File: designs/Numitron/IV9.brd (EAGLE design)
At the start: 59 x 98 mm, 13 parts, among them IC1 TLC5916IN, IC2 TLC5916IN, IC3 TLC5916IN, IC4 TLC5916IN

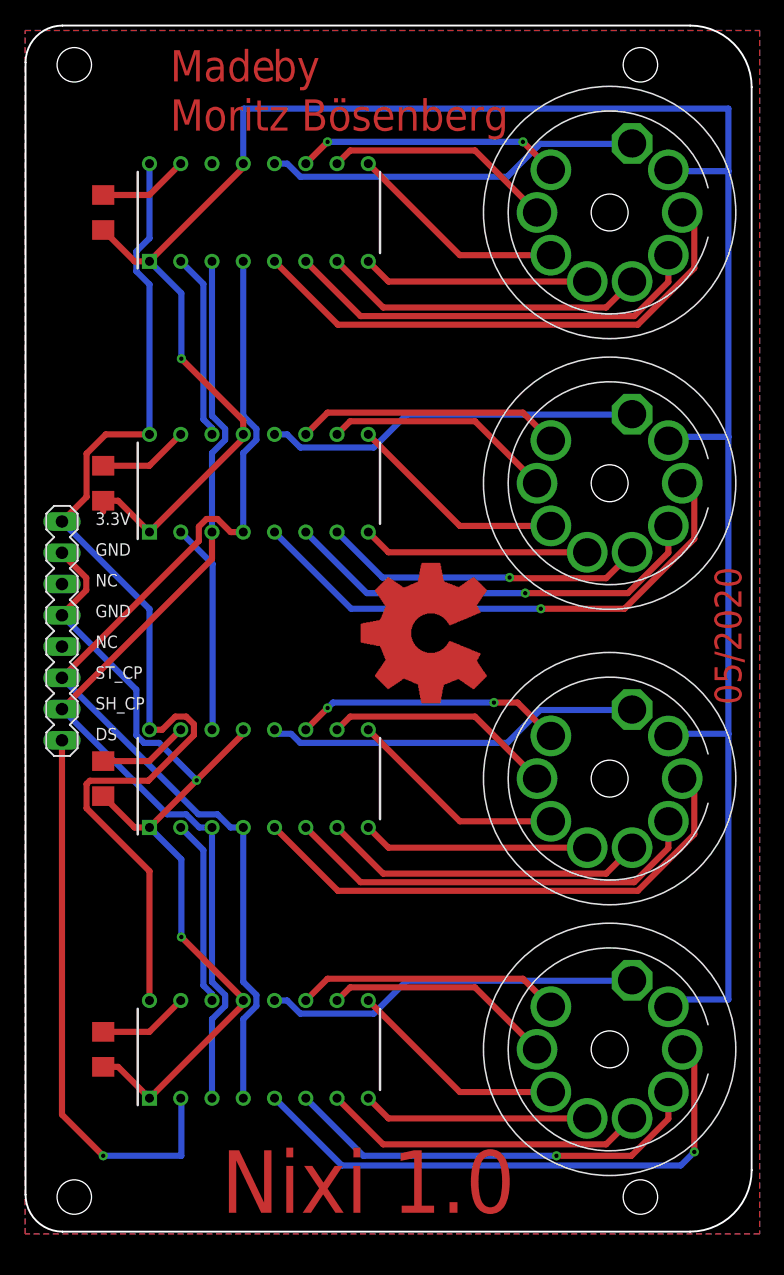
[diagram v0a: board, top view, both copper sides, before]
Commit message: added numitrons for tube clock
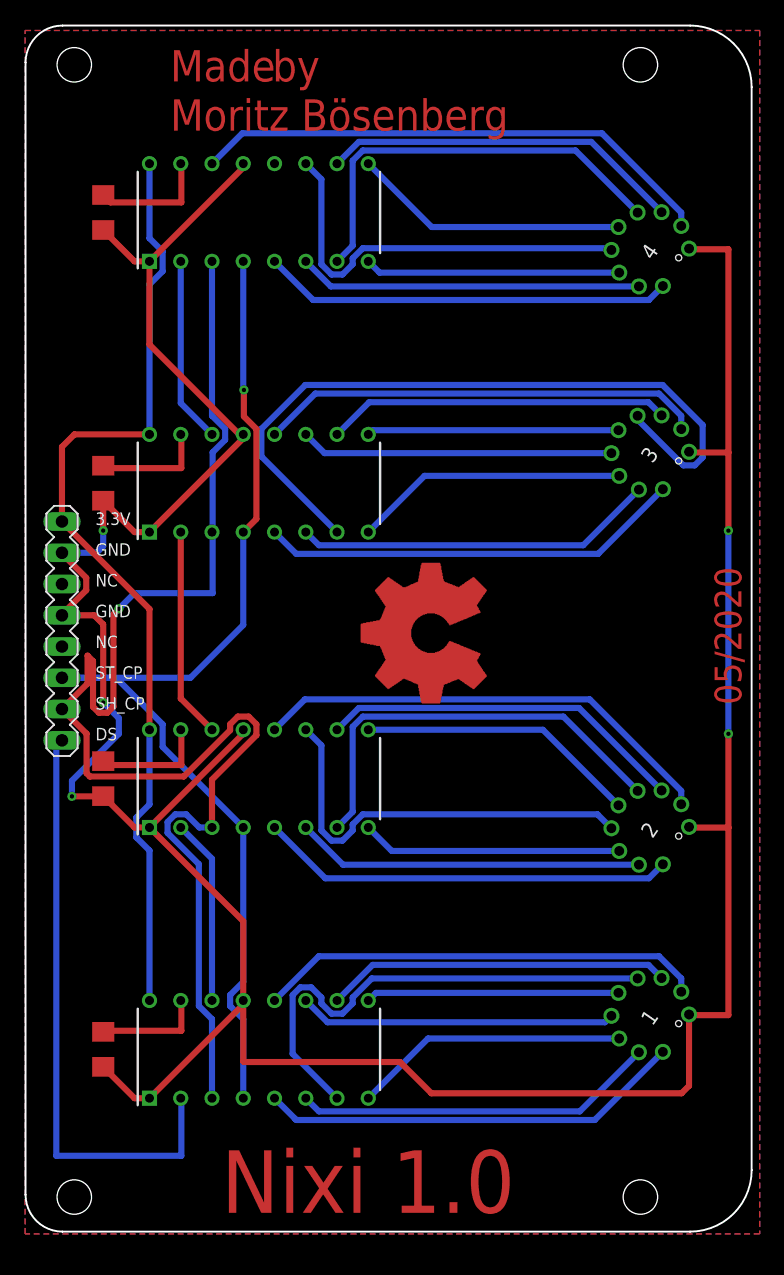
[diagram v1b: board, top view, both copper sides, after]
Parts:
- removed NUMITRON1, NUMITRON2, NUMITRON3, NUMITRON4: (no value), NixieTube:DA-2000
- added 1, 2, 3, 4: IV-9, domestichacks:IV-9
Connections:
- removed net N$1: IC3.8, NUMITRON3.6
- removed net N$10: IC1.10, NUMITRON1.8
- removed net N$11: IC1.11, NUMITRON1.9
- removed net N$12: IC2.5, NUMITRON2.3
- removed net N$14: IC2.6, NUMITRON2.4
- removed net N$2: IC3.9, NUMITRON3.7
- removed net N$3: IC1.5, NUMITRON1.3
- removed net N$33: IC2.7, NUMITRON2.5
- removed net N$34: IC2.8, NUMITRON2.6
- removed net N$37: IC2.9, NUMITRON2.7
- removed net N$38: IC2.10, NUMITRON2.8
- removed net N$39: IC2.11, NUMITRON2.9
- removed net N$4: IC1.6, NUMITRON1.4
- removed net N$40: IC3.5, NUMITRON3.3
- removed net N$41: IC3.6, NUMITRON3.4
- removed net N$42: IC3.7, NUMITRON3.5
- removed net N$43: IC4.5, NUMITRON4.3
- removed net N$44: IC4.6, NUMITRON4.4
- removed net N$45: IC3.10, NUMITRON3.8
- removed net N$46: IC3.11, NUMITRON3.9
- removed net N$47: IC4.7, NUMITRON4.5
- removed net N$5: IC1.7, NUMITRON1.5
- removed net N$50: IC4.10, NUMITRON4.8
- removed net N$51: IC4.11, NUMITRON4.9
- removed net N$6: IC1.8, NUMITRON1.6
- removed net N$7: IC4.8, NUMITRON4.6
- removed net N$8: IC1.9, NUMITRON1.7
- removed net N$9: IC4.9, NUMITRON4.7
- new net A_1: 1.5, IC1.9
- new net A_2: 2.5, IC2.9
- new net A_3: 3.5, IC3.9
- new net A_4: 4.5, IC4.9
- new net B_1: 1.3, IC1.10
- new net B_2: 2.3, IC2.10
- new net B_3: 3.3, IC3.10
- new net B_4: 4.3, IC4.10
- new net C_1: 1.4, IC1.7
- new net C_2: 2.4, IC2.7
- new net C_3: 3.4, IC3.7
- new net C_4: 4.4, IC4.7
- new net D_1: 1.8, IC1.6
- new net D_2: 2.8, IC2.6
- new net D_3: 3.8, IC3.6
- new net D_4: 4.8, IC4.6
- new net E_1: 1.9, IC1.5
- new net E_2: 2.9, IC2.5
- new net E_3: 3.9, IC3.5
- new net E_4: 4.9, IC4.5
- new net F_1: 1.6, IC1.11
- new net F_2: 2.6, IC2.11
- new net F_3: 3.6, IC3.11
- new net F_4: 4.6, IC4.11
- new net G_1: 1.7, IC1.8
- new net G_2: 2.7, IC2.8
- new net G_3: 3.7, IC3.8
- new net G_4: 4.7, IC4.8
- net DEC_1: now also 1.2; no longer NUMITRON1.1
- net DEC_2: now also 2.2; no longer NUMITRON2.1
- net DEC_3: now also 3.2; no longer NUMITRON3.1
- net DEC_4: now also 4.2, IC4.14; no longer IC4.12, NUMITRON4.1
- net GND: now also 1.1, 2.1, 3.1, 4.1; no longer NUMITRON1.2, NUMITRON2.2, NUMITRON3.2, NUMITRON4.2
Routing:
- net C_3: track 0.00 -> 59.7 mm
- net N$3: track 45.6 -> 0.00 mm, vias 1 -> 0
- net N$40: track 44.0 -> 0.00 mm, vias 1 -> 0
- net N$12: track 43.1 -> 0.00 mm
- net N$43: track 43.1 -> 0.00 mm
- net C_1: track 0.00 -> 40.8 mm
- net N$41: track 35.1 -> 0.00 mm, vias 1 -> 0
- net SH_CP: track 81.4 -> 116.4 mm, vias 0 -> 1
- net N$4: track 34.8 -> 0.00 mm, vias 1 -> 0
- net C_2: track 0.00 -> 34.7 mm
- net N$14: track 34.6 -> 0.00 mm
- net N$44: track 34.6 -> 0.00 mm
- net E_1: track 0.00 -> 34.6 mm
- net E_3: track 0.00 -> 34.5 mm
- net C_4: track 0.00 -> 34.3 mm
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
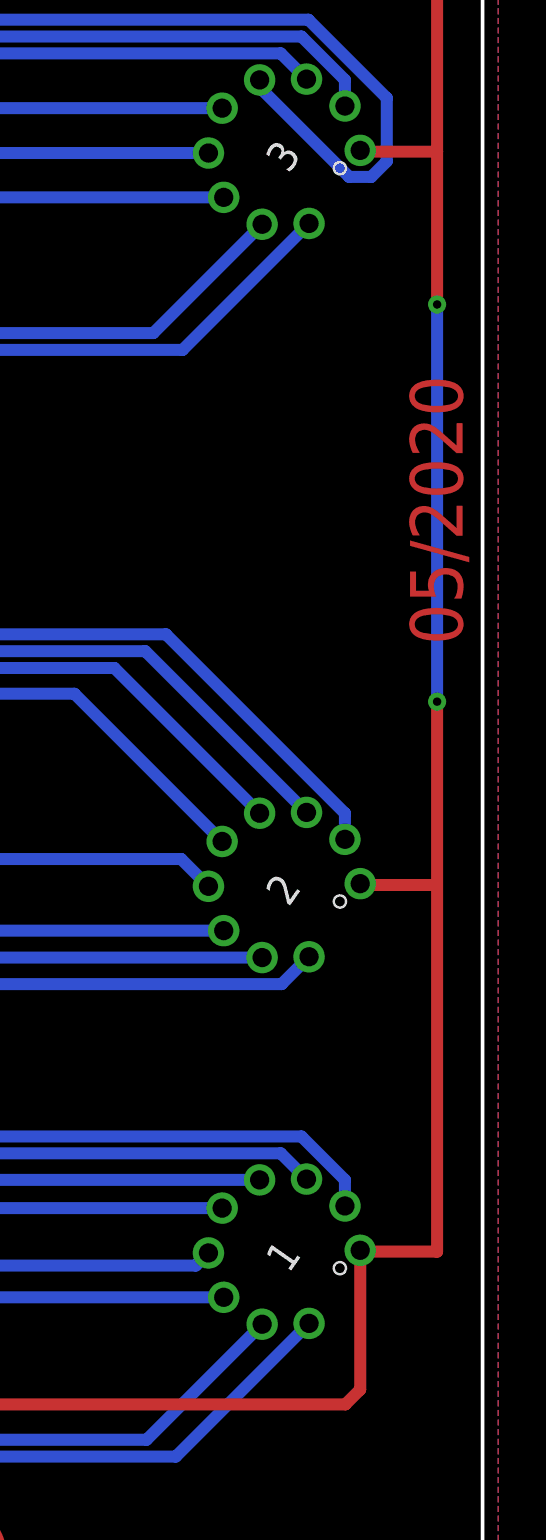
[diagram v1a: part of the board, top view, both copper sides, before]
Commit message: changes for new design excluding swap for amplifier
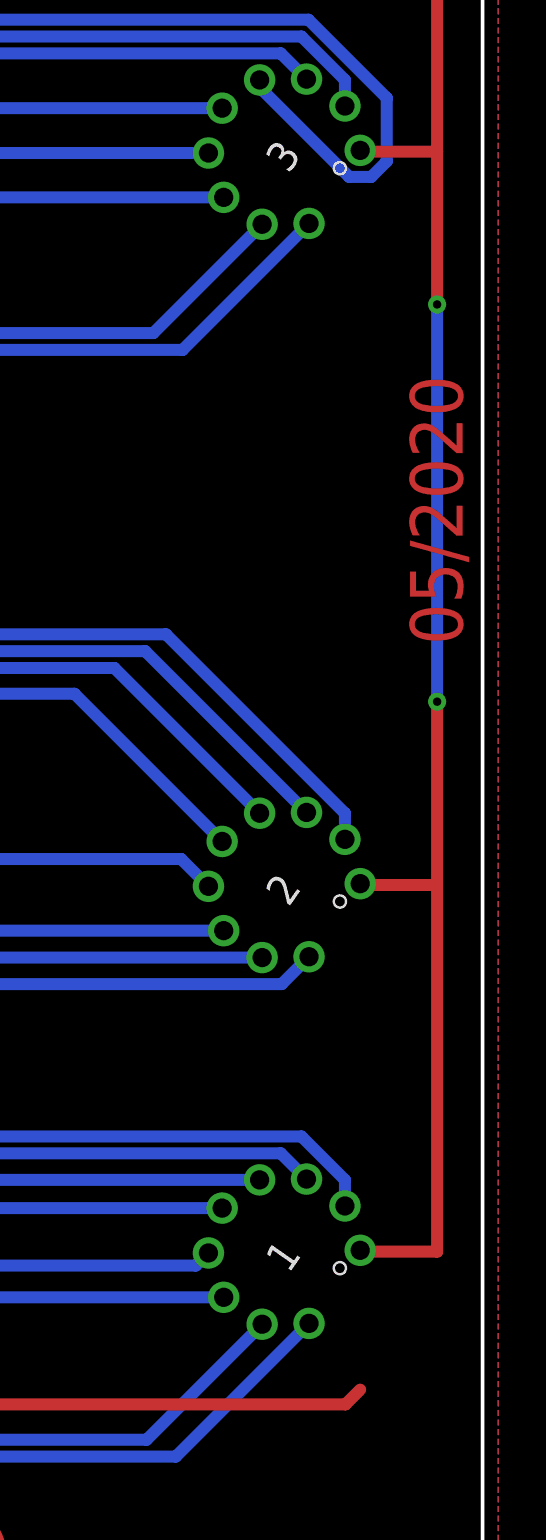
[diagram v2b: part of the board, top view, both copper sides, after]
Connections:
- net 3.3V: now also 1.1, 2.1, 3.1, 4.1
- net GND: no longer 1.1, 2.1, 3.1, 4.1
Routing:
- net GND: track 257.7 -> 176.8 mm, vias 5 -> 3
- net 3.3V: track 79.2 -> 154.1 mm, vias 0 -> 2
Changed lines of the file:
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@@
 <?xml version="1.0" encoding="utf-8"?>
 <!DOCTYPE eagle SYSTEM "eagle.dtd">
-<eagle version="9.5.2">
+<eagle version="9.6.2">
 <drawing>
 <settings>
@@
 </layers>
 <board>
-<fusionsync huburn="a.cGVyc29uYWw6dWUyYTNmMDU1" projecturn="a.cGVyc29uYWw6dWUyYTNmMDU1IzIwMTgxMjEwMTY0OTQ5MjI2" f3durn="urn:adsk.wipprod:dm.lineage:4MC1XJpNS5OembdtZ6758A" pcbguid="e03bb4f2-0a4d-4210-a02e-cfae97411f01" lastpulledtime="" lastsyncedchangeguid="06026abe-28e3-6ea0-b32c-c76c4e3af893"/>
+<fusionsync huburn="a.cGVyc29uYWw6dWUyYTNmMDU1" projecturn="a.cGVyc29uYWw6dWUyYTNmMDU1IzIwMTgxMjEwMTY0OTQ5MjI2" f3durn="urn:adsk.wipprod:dm.lineage:4MC1XJpNS5OembdtZ6758A" pcbguid="e03bb4f2-0a4d-4210-a02e-cfae97411f01" lastpulledtime="" lastsyncedchangeguid="06026abe-28e3-6ea0-b32c-c76c4e3af893" latestrevisionid="" lastsyncedrevisionid="" lastboardhashguid="" lastpushedtime="" linktopcb3d="false"/>
 <plain>
 <wire x1="3.04" y1="98.19" x2="54.04" y2="98.19" width="0.1524" layer="20"/>
@@
 <contactref element="SV2" pad="5"/>
 <contactref element="SV2" pad="7"/>
-<contactref element="1" pad="1"/>
-<contactref element="2" pad="1"/>
-<contactref element="3" pad="1"/>
-<contactref element="4" pad="1"/>
-<wire x1="53.95394375" y1="80.065021875" x2="54.008965625" y2="80.01" width="0.5" layer="1"/>
-<wire x1="54.008965625" y1="80.01" x2="57.15" y2="80.01" width="0.5" layer="1"/>
-<wire x1="57.15" y1="80.01" x2="57.15" y2="63.5" width="0.5" layer="1"/>
-<via x="57.15" y="57.15" extent="1-16" drill="0.35"/>
-<wire x1="57.15" y1="63.5" x2="57.15" y2="57.15" width="0.5" layer="1"/>
-<wire x1="57.15" y1="57.15" x2="57.15" y2="40.64" width="0.5" layer="16"/>
-<via x="57.15" y="40.64" extent="1-16" drill="0.35"/>
-<wire x1="57.15" y1="40.64" x2="57.15" y2="33.02" width="0.5" layer="1"/>
-<wire x1="57.15" y1="33.02" x2="57.15" y2="17.78" width="0.5" layer="1"/>
-<wire x1="57.15" y1="17.78" x2="54.008965625" y2="17.78" width="0.5" layer="1"/>
-<wire x1="54.008965625" y1="17.78" x2="53.95394375" y2="17.835021875" width="0.5" layer="1"/>
-<wire x1="53.95394375" y1="33.075021875" x2="54.008965625" y2="33.02" width="0.5" layer="1"/>
-<wire x1="54.008965625" y1="33.02" x2="57.15" y2="33.02" width="0.5" layer="1"/>
-<wire x1="53.95394375" y1="63.555021875" x2="54.008965625" y2="63.5" width="0.5" layer="1"/>
-<wire x1="54.008965625" y1="63.5" x2="57.15" y2="63.5" width="0.5" layer="1"/>
 <wire x1="6.35" y1="13.578" x2="8.898" y2="11.03" width="0.5" layer="1"/>
 <wire x1="8.898" y1="11.03" x2="10.11" y2="11.03" width="0.5" layer="1"/>
@@
 <wire x1="10.11" y1="11.03" x2="17.73" y2="18.65" width="0.5" layer="1"/>
 <wire x1="17.73" y1="18.65" x2="17.73" y2="18.97" width="0.5" layer="1"/>
-<wire x1="53.95394375" y1="17.835021875" x2="53.95394375" y2="12.04394375" width="0.5" layer="1"/>
 <wire x1="53.95394375" y1="12.04394375" x2="53.34" y2="11.43" width="0.5" layer="1"/>
 <wire x1="53.34" y1="11.43" x2="33.02" y2="11.43" width="0.5" layer="1"/>
@@
 <wire x1="10.11" y1="80.90439375" x2="11.179" y2="79.83539375" width="0.5" layer="16"/>
 <wire x1="11.179" y1="78.22460625" x2="10.11" y2="77.15560625" width="0.5" layer="16"/>
+<contactref element="1" pad="1"/>
+<contactref element="2" pad="1"/>
+<contactref element="3" pad="1"/>
+<contactref element="4" pad="1"/>
+<wire x1="53.95394375" y1="80.065021875" x2="54.008965625" y2="80.01" width="0.5" layer="1"/>
+<wire x1="54.008965625" y1="80.01" x2="57.15" y2="80.01" width="0.5" layer="1"/>
+<wire x1="57.15" y1="80.01" x2="57.15" y2="63.5" width="0.5" layer="1"/>
+<via x="57.15" y="57.15" extent="1-16" drill="0.35"/>
+<wire x1="57.15" y1="63.5" x2="57.15" y2="57.15" width="0.5" layer="1"/>
+<wire x1="57.15" y1="57.15" x2="57.15" y2="40.64" width="0.5" layer="16"/>
+<via x="57.15" y="40.64" extent="1-16" drill="0.35"/>
+<wire x1="57.15" y1="40.64" x2="57.15" y2="33.02" width="0.5" layer="1"/>
+<wire x1="57.15" y1="33.02" x2="57.15" y2="17.78" width="0.5" layer="1"/>
+<wire x1="57.15" y1="17.78" x2="54.008965625" y2="17.78" width="0.5" layer="1"/>
+<wire x1="54.008965625" y1="33.02" x2="57.15" y2="33.02" width="0.5" layer="1"/>
+<wire x1="54.008965625" y1="63.5" x2="57.15" y2="63.5" width="0.5" layer="1"/>
+<wire x1="54.008965625" y1="63.5" x2="53.95394375" y2="63.555021875" width="0" layer="19" extent="1-1"/>
+<wire x1="53.95394375" y1="33.075021875" x2="54.008965625" y2="33.02" width="0" layer="19" extent="1-1"/>
+<wire x1="53.95394375" y1="17.835021875" x2="54.008965625" y2="17.78" width="0" layer="19" extent="1-1"/>
+<wire x1="10.11" y1="64.97" x2="53.95394375" y2="63.555021875" width="0" layer="19" extent="1-1"/>
 </signal>
 <signal name="R-EXT4">
